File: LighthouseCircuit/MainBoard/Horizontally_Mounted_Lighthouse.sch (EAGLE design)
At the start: 23 parts

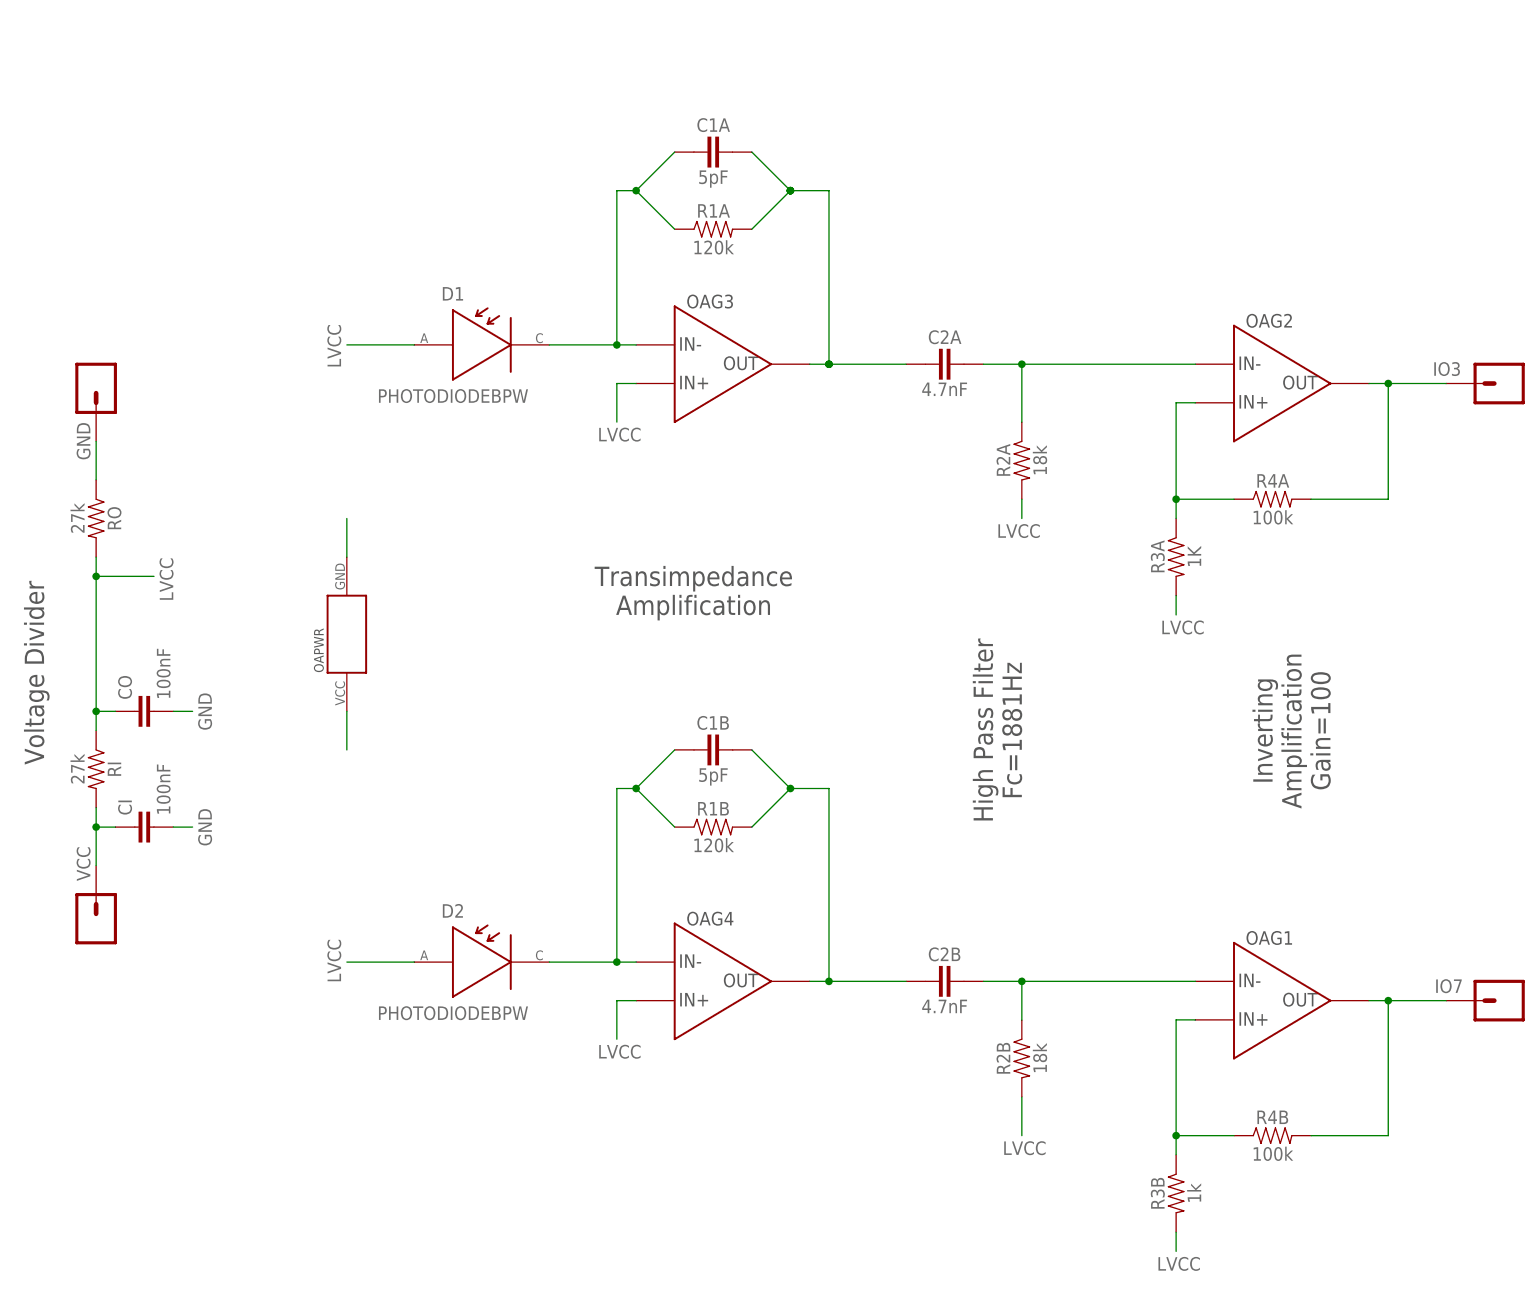
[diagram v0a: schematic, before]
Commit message: Progress toward using bi-arc computations for execution of path following.
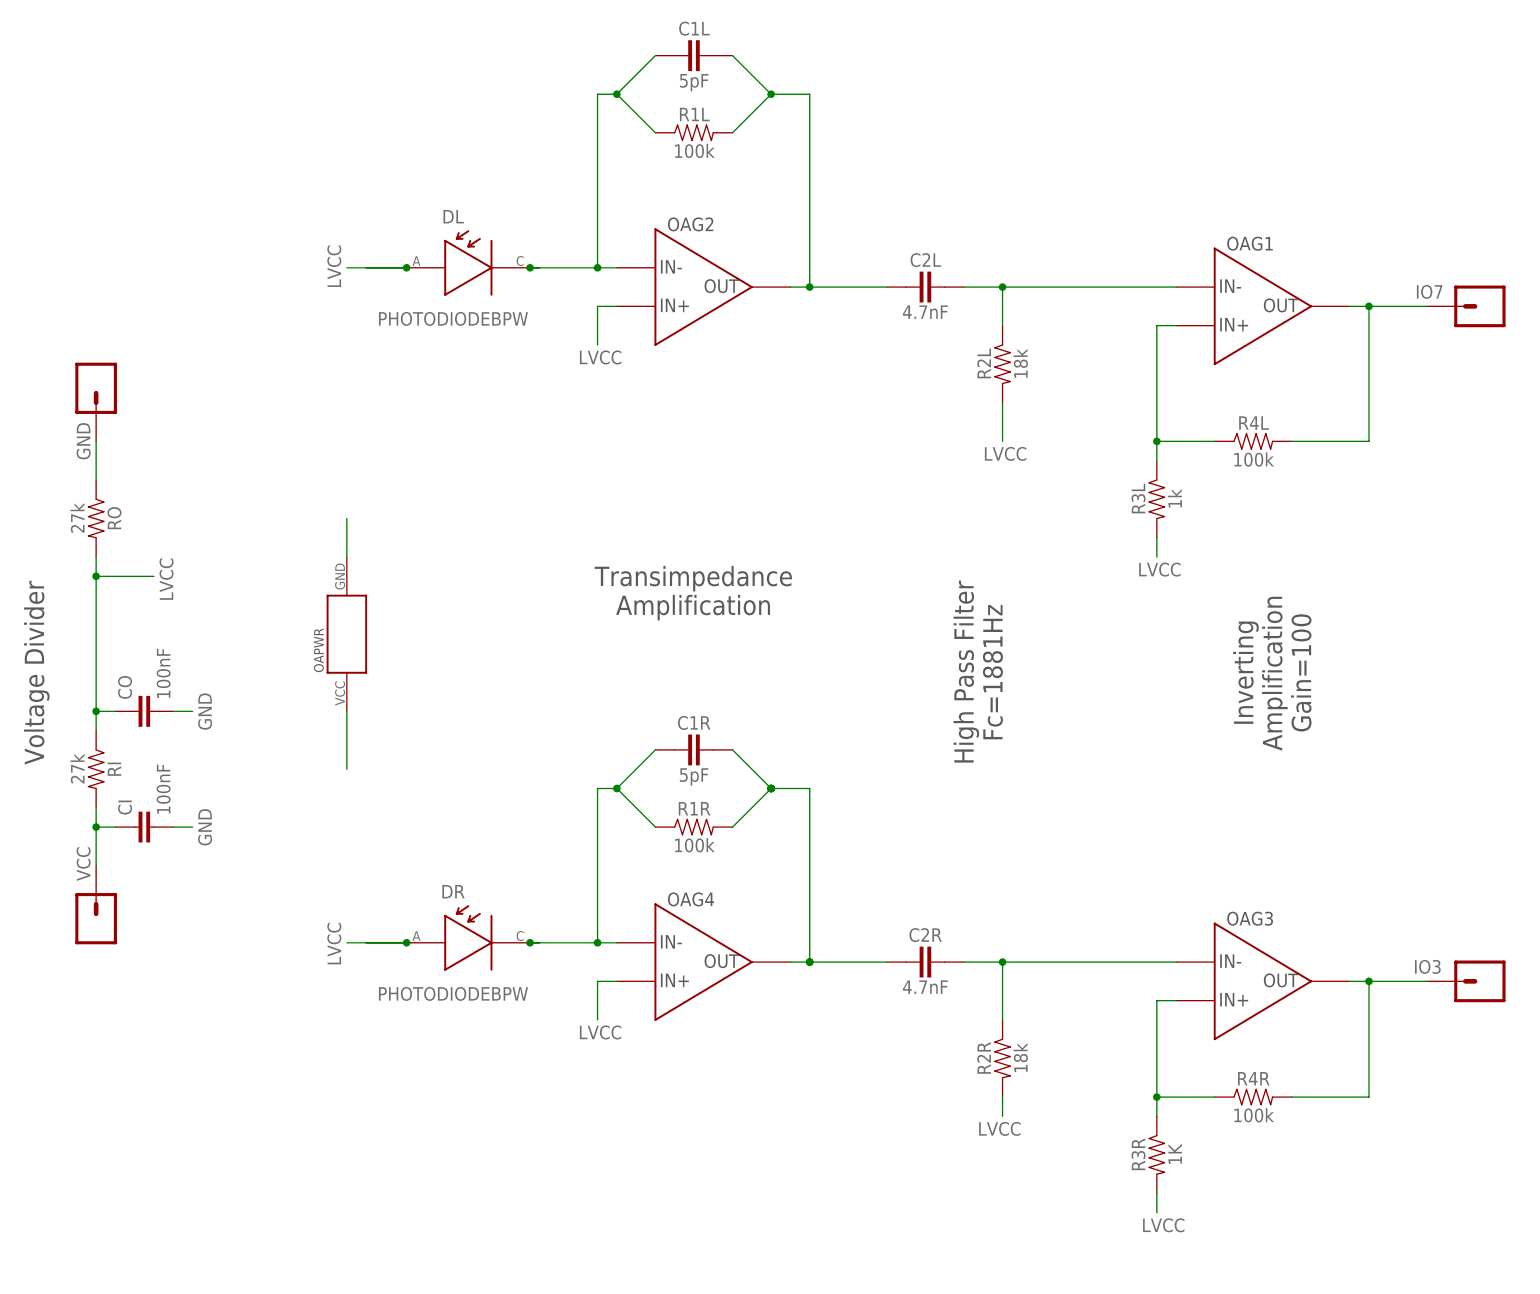
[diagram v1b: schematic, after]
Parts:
- removed C1A, C1B: 5pF, ZippyComponentLibrary:CAPACITOR
- removed C2A, C2B: 4.7nF, ZippyComponentLibrary:CAPACITOR
- removed D1, D2: PHOTODIODEBPW, ZippyComponentLibrary:PHOTODIODEBPW
- removed R1A, R1B: 120k, ZippyComponentLibrary:RESISTOR
- removed R2A, R2B: 18k, ZippyComponentLibrary:RESISTOR
- removed R3A: 1K, ZippyComponentLibrary:RESISTOR
- removed R3B: 1k, ZippyComponentLibrary:RESISTOR
- removed R4A, R4B: 100k, ZippyComponentLibrary:RESISTOR
- added C1L, C1R: 5pF, ZippyComponentLibrary:CAPACITOR
- added C2L, C2R: 4.7nF, ZippyComponentLibrary:CAPACITOR
- added DL, DR: PHOTODIODEBPW, ZippyComponentLibrary:PHOTODIODEBPW
- added R1L, R1R, R4L, R4R: 100k, ZippyComponentLibrary:RESISTOR
- added R2L, R2R: 18k, ZippyComponentLibrary:RESISTOR
- added R3L: 1k, ZippyComponentLibrary:RESISTOR
- added R3R: 1K, ZippyComponentLibrary:RESISTOR
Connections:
- removed net D1IN: C1B.1, D2.CATHODE, OAG4.IN-, R1B.1
- removed net D1OA2P: C2B.2, OAG1.IN-, R2B.1
- removed net D1OAOUT1: C1B.2, C2B.1, OAG4.OUT, R1B.2
- removed net D2IN: C1A.1, D1.CATHODE, OAG3.IN-, R1A.1
- removed net D2OA1OUT: C1A.2, C2A.1, OAG3.OUT, R1A.2
- removed net D2OA2N: OAG2.IN+, R3A.1, R4A.1
- removed net D2OA2P: C2A.2, OAG2.IN-, R2A.1
- removed net N$11: OAG1.IN+, R3B.1, R4B.1
- new net DL1IN: C1L.1, DL.CATHODE, OAG2.IN-, R1L.1
- new net DL1OUT: C1L.2, C2L.1, OAG2.OUT, R1L.2
- new net DL2F: OAG1.IN+, R3L.1, R4L.1
- new net DL2IN: C2L.2, OAG1.IN-, R2L.1
- new net DR1IN: C1R.1, DR.CATHODE, OAG4.IN-, R1R.1
- new net DR1OUT: C1R.2, C2R.1, OAG4.OUT, R1R.2
- new net DR2F: OAG3.IN+, R3R.1, R4R.1
- new net DR2IN: C2R.2, OAG3.IN-, R2R.1
- net IO3: now also OAG3.OUT, R4R.2; no longer OAG2.OUT, R4A.2
- net IO7: now also R4L.2; no longer R4B.2
- net LVCC: now also DL.ANODE, DR.ANODE, OAG2.IN+, R2L.2, R2R.2, R3L.2, R3R.2; no longer D1.ANODE, D2.ANODE, OAG3.IN+, R2A.2, R2B.2, R3A.2, R3B.2
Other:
- moved on the sheet: OAG1, OAG2, OAG3, OAG4
